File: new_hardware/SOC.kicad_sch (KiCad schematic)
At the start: 96 parts, among them J1 TF01-A, P1 WF24LTYAJDNN0#, P2 USB-TYPE-C-018, Q1 2N7002K, SW1 K2-1156SP-F5SW-05, SW2 K2-1156SP-F5SW-05, SW3 K2-1156SP-F5SW-05, SW4 K2-1156SP-F5SW-05, SW5 K2-1156SP-F5SW-05, SW6 GT-TC054A-H035-L1, SW7 GT-TC054A-H035-L1, U1 F133, U2 USBLC6-2SC6, U3 MX25L25645GM2I-08G, Y1 12.88727

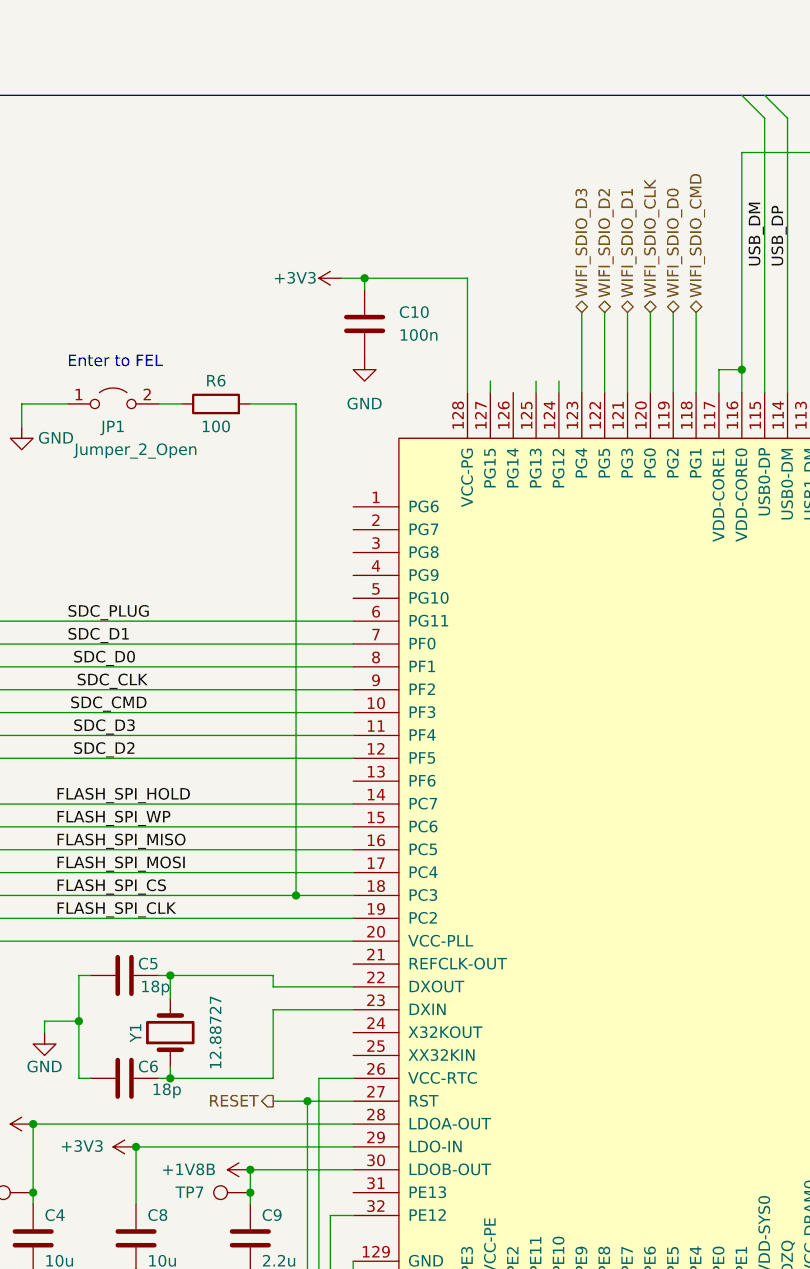
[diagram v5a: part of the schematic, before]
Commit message: wi-fi module is moved to closer board outline,unused files are removed
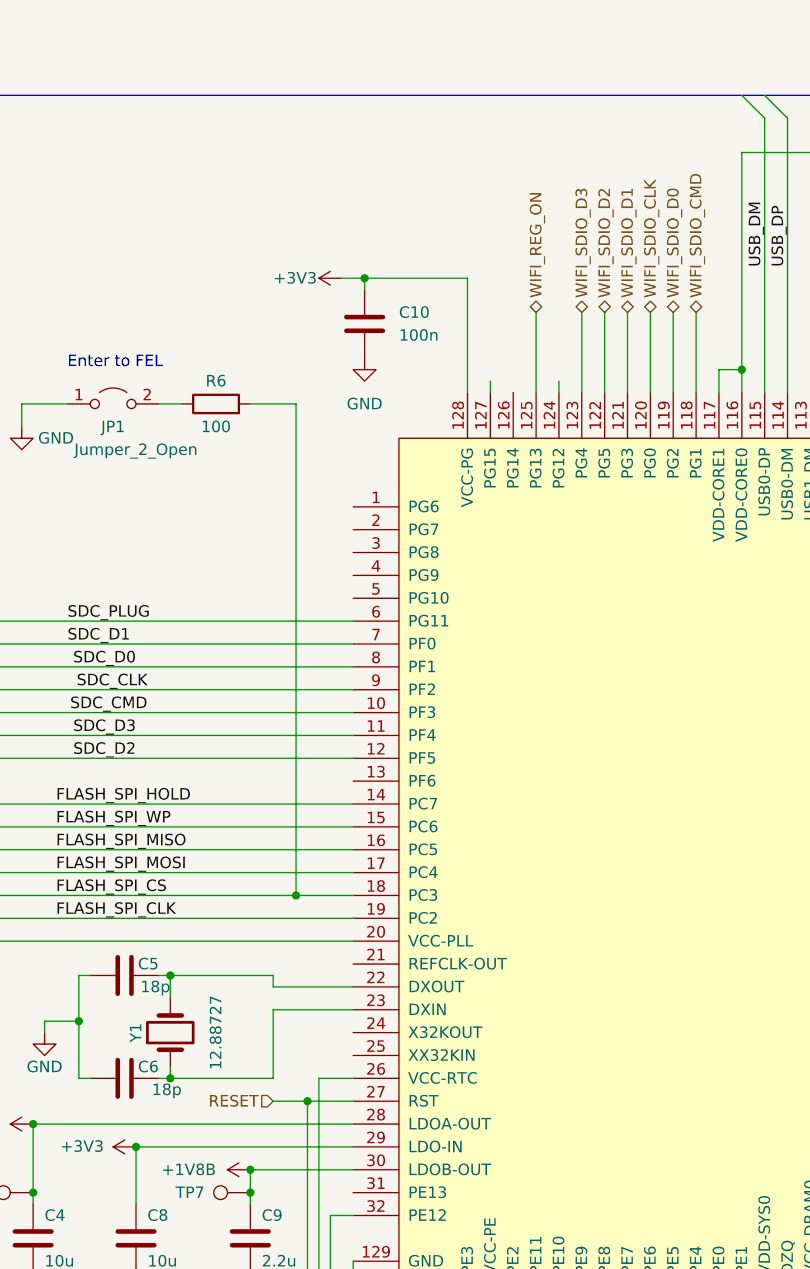
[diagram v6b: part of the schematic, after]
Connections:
- net WIFI_REG_ON: now reaches U1.125 (PG13)
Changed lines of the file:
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@@
     (stroke (width 0) (type default) (color 0 0 0 0))
   )
-  (wire (pts (xy 153.67 71.12) (xy 153.67 72.39))
+  (wire (pts (xy 153.67 63.5) (xy 153.67 72.39))
     (stroke (width 0) (type default) (color 0 0 0 0))
   )
@@
     )
   )
+  (hierarchical_label "WIFI_REG_ON" (shape bidirectional) (at 153.67 63.5 90)
+    (effects (font (size 1.27 1.27)) (justify left))
+  )
   (hierarchical_label "I2S_DOUT" (shape input) (at 242.57 115.57 0)
     (effects (font (size 1.27 1.27)) (justify left))
@@
     (effects (font (size 1.27 1.27)) (justify left))
   )
-  (hierarchical_label "RESET" (shape output) (at 124.46 151.13 180)
+  (hierarchical_label "RESET" (shape input) (at 124.46 151.13 180)
     (effects (font (size 1.27 1.27)) (justify right))
   )
